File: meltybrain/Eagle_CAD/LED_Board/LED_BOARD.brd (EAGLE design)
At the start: 56.4 x 10 mm, 17 parts, among them J1 SM04B-SRSS-TB(LF)(SN)

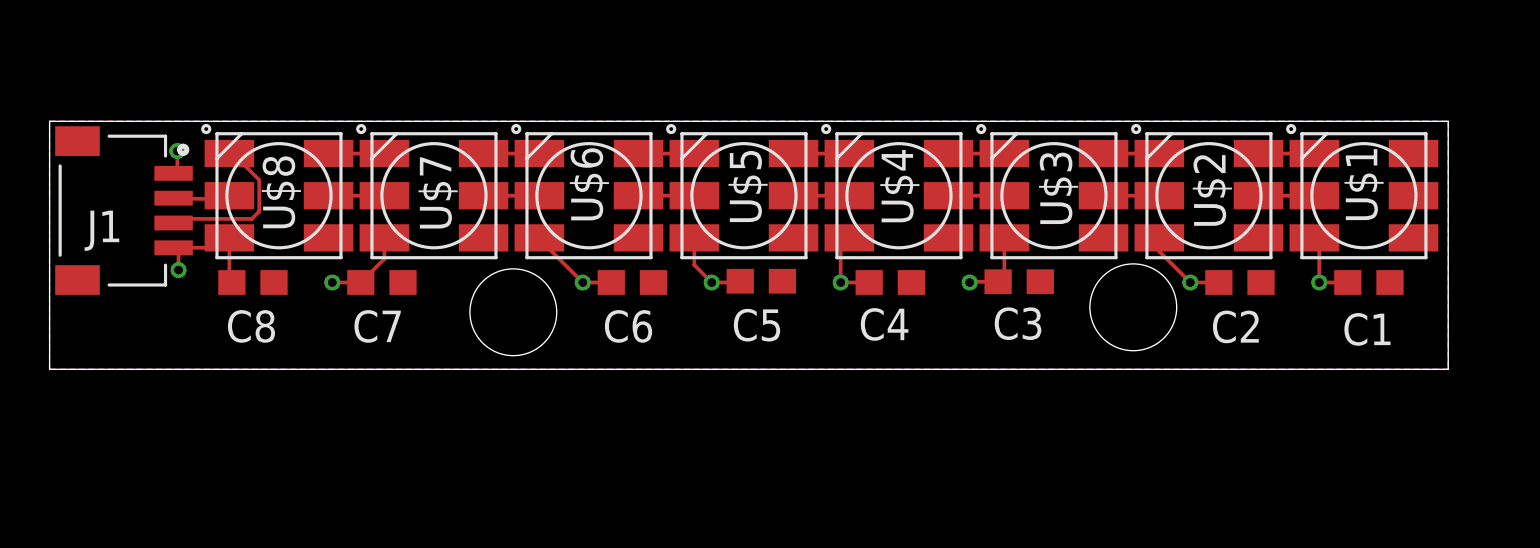
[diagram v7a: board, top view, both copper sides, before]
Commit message: Changes to led board
adjusted screw holes
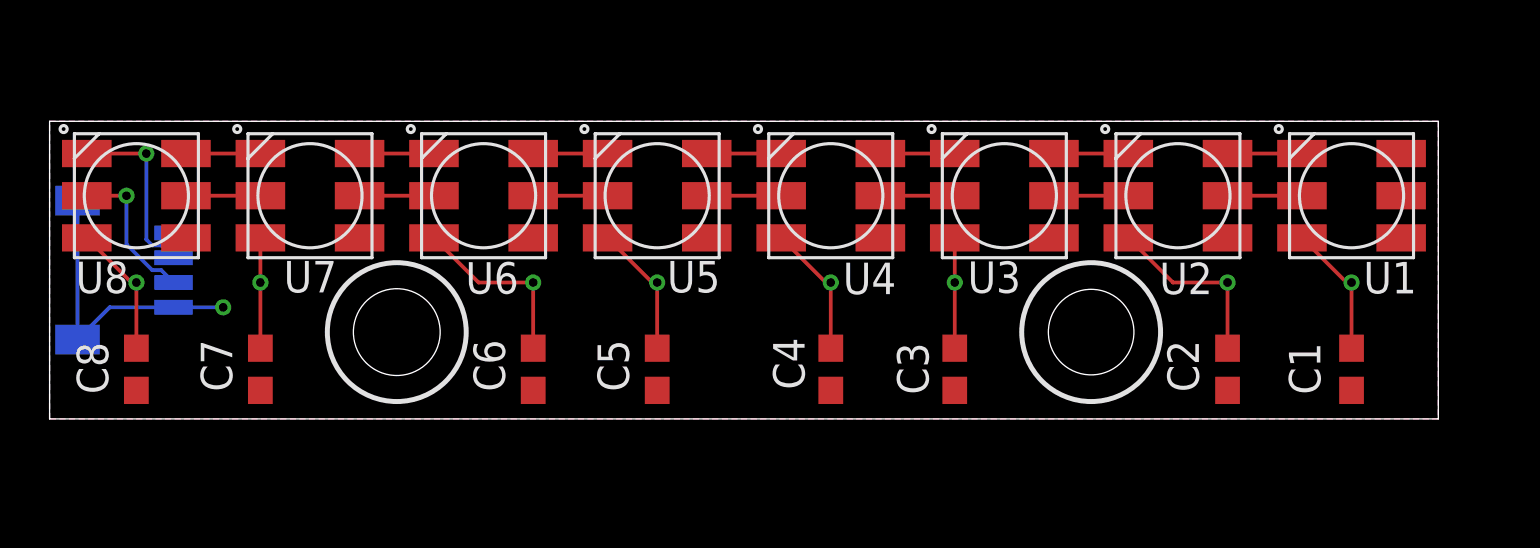
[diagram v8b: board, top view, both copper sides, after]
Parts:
- removed U$1, U$2, U$3, U$4, U$5, U$6, U$7, U$8: DOTSTAR, LED_BOARD:RGBLED5050
- added U1, U2, U3, U4, U5, U6, U7, U8: DOTSTAR, LED_BOARD:RGBLED5050
- moved C7 6.02 mm to (8.50, 0.00), turned to 90 degrees
- moved C8 5.86 mm to (3.50, 0.00), turned to 90 degrees
- moved C5 5.50 mm to (24.5, 0.00), turned to 90 degrees
- moved C6 5.32 mm to (19.5, 0.00), turned to 90 degrees
- moved C3 4.38 mm to (36.5, 0.00), turned to 90 degrees
- moved C4 4.24 mm to (31.5, 0.00), turned to 90 degrees
- moved C1 3.57 mm to (52.5, 0.00), turned to 90 degrees
- moved C2 3.54 mm to (47.5, 0.00), turned to 90 degrees
- moved J1 2.40 mm to (5.00, 4.00), flipped to the bottom, turned to 90 degrees
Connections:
- net +5V: now also J1.S1, J1.S2, U1.4, U2.4, U3.4, U4.4, U5.4, U6.4, U7.4, U8.4; no longer U$1.4, U$2.4, U$3.4, U$4.4, U$5.4, U$6.4, U$7.4, U$8.4
- net GND: now also U1.3, U2.3, U3.3, U4.3, U5.3, U6.3, U7.3, U8.3; no longer U$1.3, U$2.3, U$3.3, U$4.3, U$5.3, U$6.3, U$7.3, U$8.3
- net N$1: now also U1.2, U2.5; no longer U$1.2, U$2.5
- net N$10: now also U5.1, U6.6; no longer U$5.1, U$6.6
- net N$11: now also U6.2, U7.5; no longer U$6.2, U$7.5
- net N$12: now also U6.1, U7.6; no longer U$6.1, U$7.6
- net N$13: now also U7.2, U8.5; no longer U$7.2, U$8.5
- net N$14: now also U7.1, U8.6; no longer U$7.1, U$8.6
- net N$15: now also U8.2; no longer U$8.2
- net N$16: now also U8.1; no longer U$8.1
- net N$2: now also U1.1, U2.6; no longer U$1.1, U$2.6
- net N$3: now also U2.2, U3.5; no longer U$2.2, U$3.5
- net N$4: now also U2.1, U3.6; no longer U$2.1, U$3.6
- net N$5: now also U3.2, U4.5; no longer U$3.2, U$4.5
- net N$6: now also U3.1, U4.6; no longer U$3.1, U$4.6
- net N$7: now also U4.2, U5.5; no longer U$4.2, U$5.5
- net N$8: now also U4.1, U5.6; no longer U$4.1, U$5.6
- net N$9: now also U5.2, U6.5; no longer U$5.2, U$6.5
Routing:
- net GND: track 28.2 -> 45.3 mm
- net +5V: track 1.40 -> 12.0 mm
- net N$15: track 2.29 -> 6.10 mm, vias 0 -> 1
- net N$9: track 2.25 -> 3.00 mm
- net N$8: track 2.25 -> 3.00 mm
- net N$7: track 2.25 -> 3.00 mm
- net N$6: track 2.25 -> 3.00 mm
- net N$5: track 2.25 -> 3.00 mm
- net N$4: track 2.25 -> 3.00 mm
- net N$3: track 2.25 -> 3.00 mm
- net N$2: track 2.25 -> 3.00 mm
- net N$14: track 2.25 -> 3.00 mm
- net N$13: track 2.25 -> 3.00 mm
- net N$12: track 2.25 -> 3.00 mm
- net N$11: track 2.25 -> 3.00 mm
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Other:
- board size 56.4 x 10 mm -> 56 x 12 mm
